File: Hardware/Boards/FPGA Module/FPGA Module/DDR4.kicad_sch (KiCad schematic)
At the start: 36 parts, among them U17 MT40A512M16LY-075:E, U9 TPS74801AWDRC

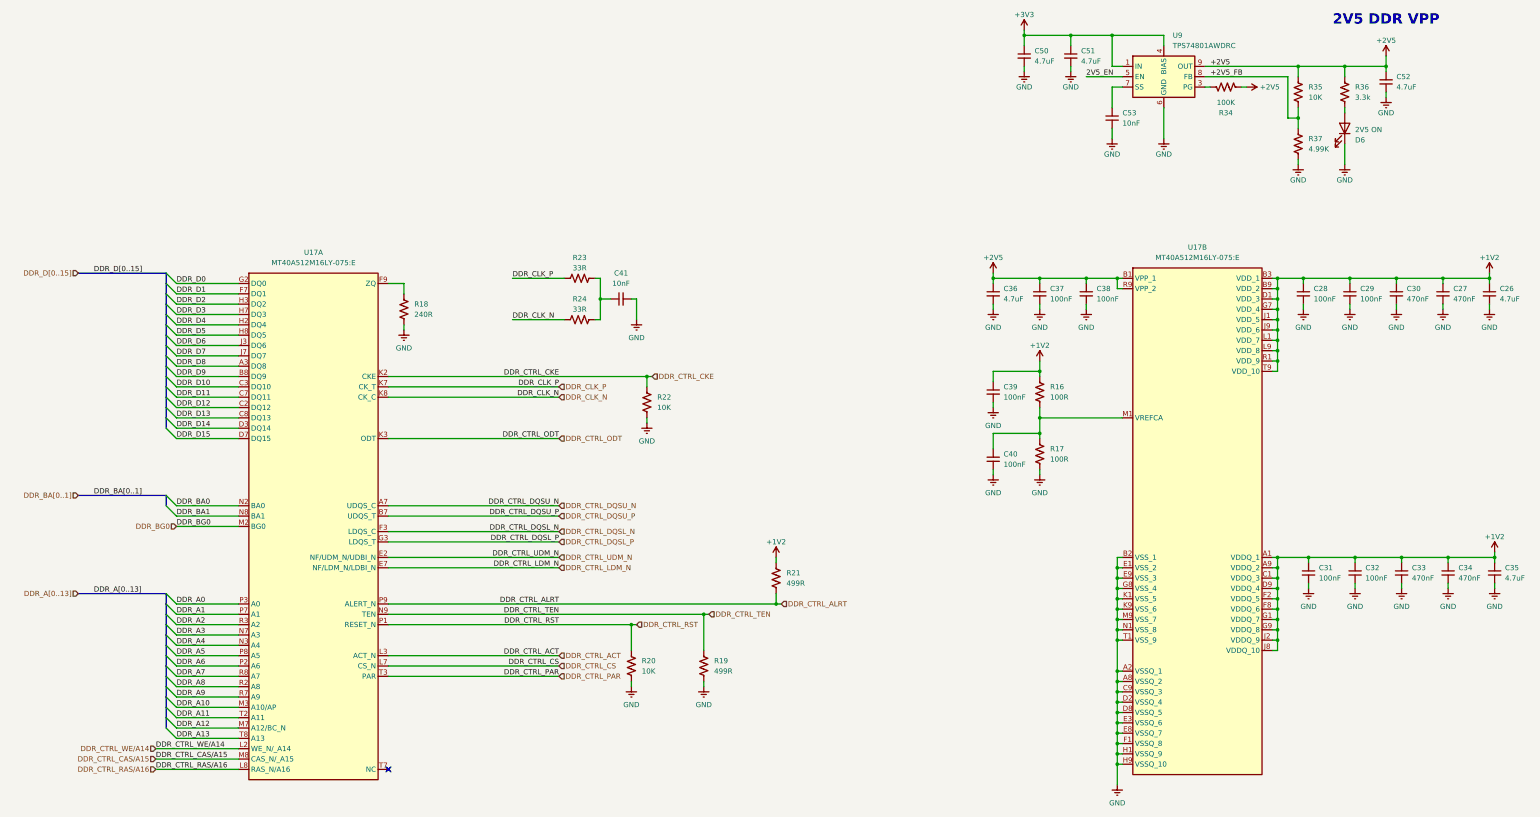
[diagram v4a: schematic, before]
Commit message: Update FPGA Module Netclasses
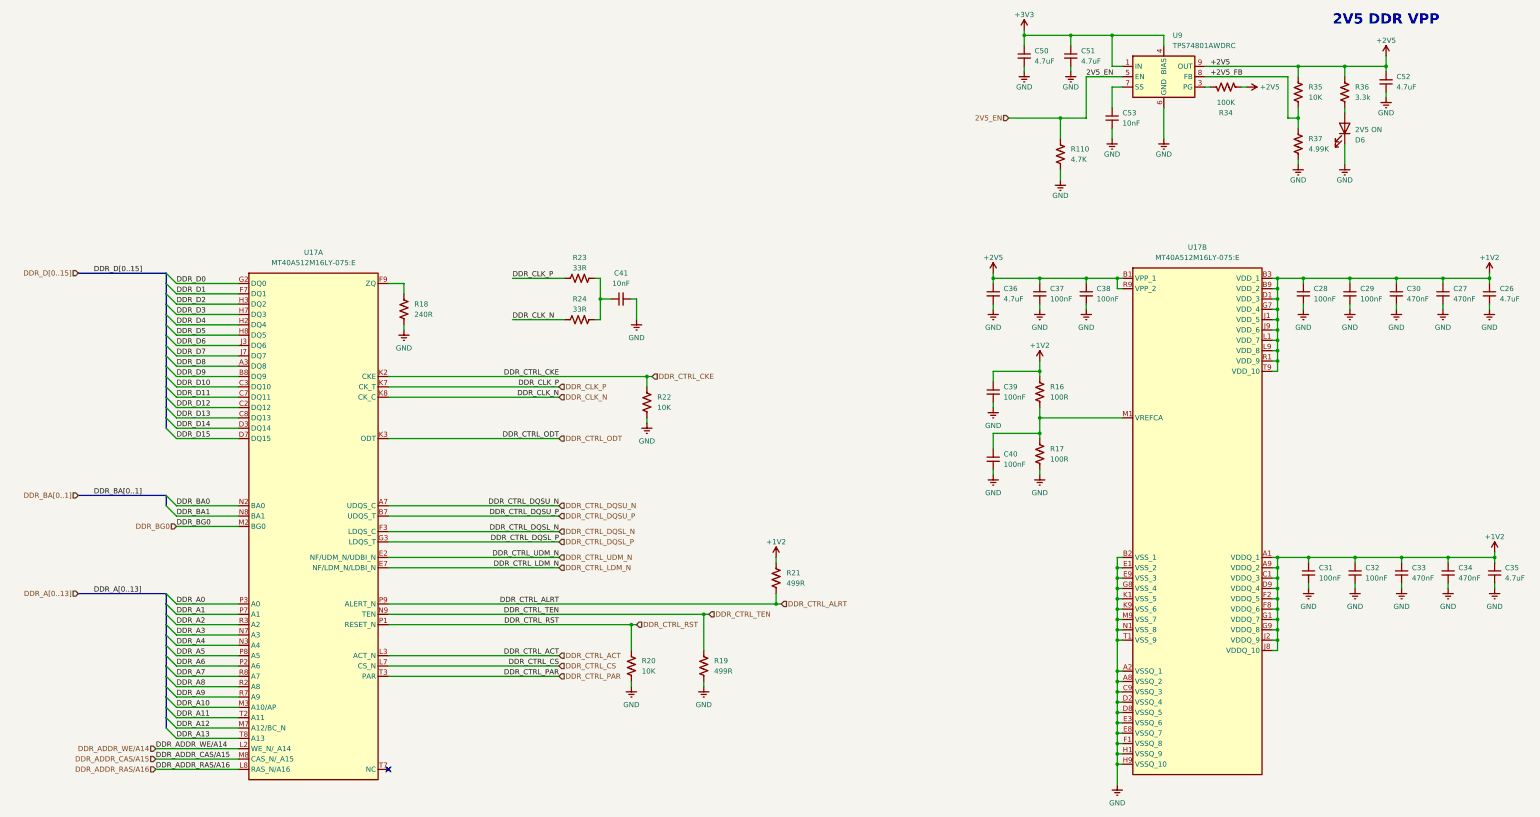
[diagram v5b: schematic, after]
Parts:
- added R110: 4.7K, Resistor_SMD:R_0402_1005Metric, symbol Device:R_US
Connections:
- net 2V5_EN: now also R110.2
- net GND: now also R110.1
- net DDR_CTRL_CAS/A15 renamed DDR_ADDR_CAS/A15
- net DDR_CTRL_RAS/A16 renamed DDR_ADDR_RAS/A16
- net DDR_CTRL_WE/A14 renamed DDR_ADDR_WE/A14
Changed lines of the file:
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@@
 	)
 	(junction
+		(at 279.4 53.34)
+		(diameter 0)
+		(color 0 0 0 0)
+	)
+	(junction
 		(at 293.37 191.77)
 		(diameter 0)
@@
 	(wire
 		(pts
+			(xy 279.4 53.34) (xy 285.75 53.34)
+		)
+		(stroke
+			(width 0)
+			(type default)
+		)
+	)
+	(wire
+		(pts
 			(xy 332.74 166.37) (xy 332.74 168.91)
 		)
@@
 	(wire
 		(pts
+			(xy 266.7 53.34) (xy 279.4 53.34)
+		)
+		(stroke
+			(width 0)
+			(type default)
+		)
+	)
+	(wire
+		(pts
 			(xy 62.23 185.42) (xy 77.47 185.42)
 		)
@@
 	(wire
 		(pts
+			(xy 279.4 66.04) (xy 279.4 68.58)
+		)
+		(stroke
+			(width 0)
+			(type default)
+		)
+	)
+	(wire
+		(pts
 			(xy 337.82 53.34) (xy 337.82 50.8)
 		)
@@
 	(wire
 		(pts
+			(xy 279.4 53.34) (xy 279.4 58.42)
+		)
+		(stroke
+			(width 0)
+			(type default)
+		)
+	)
+	(wire
+		(pts
 			(xy 166.37 102.87) (xy 165.1 102.87)
 		)
@@
 		)
 	)
+	(wire
+		(pts
+			(xy 285.75 53.34) (xy 285.75 43.18)
+		)
+		(stroke
+			(width 0)
+			(type default)
+		)
+	)
 	(bus
 		(pts
@@
 		)
 	)
-	(label "DDR_CTRL_CAS{slash}A15"
+	(label "DDR_ADDR_CAS{slash}A15"
 		(at 57.15 210.82 0)
 		(fields_autoplaced yes)
@@
 		)
 	)
-	(label "DDR_CTRL_RAS{slash}A16"
+	(label "DDR_ADDR_RAS{slash}A16"
 		(at 57.15 213.36 0)
 		(fields_autoplaced yes)
@@
 		)
 	)
-	(label "DDR_CTRL_WE{slash}A14"
+	(label "DDR_ADDR_WE{slash}A14"
 		(at 57.15 208.28 0)
 		(fields_autoplaced yes)
@@
 		)
 	)
-	(hierarchical_label "DDR_CTRL_RAS{slash}A16"
+	(hierarchical_label "DDR_ADDR_RAS{slash}A16"
 		(shape input)
 		(at 57.15 213.36 180)
@@
 		)
 	)
-	(hierarchical_label "DDR_CTRL_CAS{slash}A15"
+	(hierarchical_label "DDR_ADDR_CAS{slash}A15"
 		(shape input)
 		(at 57.15 210.82 180)
@@
 		)
 	)
-	(hierarchical_label "DDR_CTRL_WE{slash}A14"
+	(hierarchical_label "DDR_ADDR_WE{slash}A14"
 		(shape input)
 		(at 57.15 208.28 180)
@@
 		)
 	)
+	(hierarchical_label "2V5_EN"
+		(shape input)
+		(at 266.7 53.34 180)
+		(fields_autoplaced yes)
+		(effects
+			(font
+				(size 1.27 1.27)
+			)
+			(justify right)
+		)
+	)
 	(hierarchical_label "DDR_D[0..15]"
 		(shape input)
@@
 	)
 	(symbol
+		(lib_id "Device:R_US")
+		(at 279.4 62.23 180)
+		(unit 1)
+		(exclude_from_sim no)
+		(in_bom yes)
+		(on_board yes)
+		(dnp no)
+		(fields_autoplaced yes)
+		(property "Reference" "R110"
+			(at 281.94 60.9599 0)
+			(effects
+				(font
+					(size 1.27 1.27)
+				)
+				(justify right)
+			)
+		)
+		(property "Value" "4.7K"
+			(at 281.94 63.4999 0)
+			(effects
+				(font
+					(size 1.27 1.27)
+				)
+				(justify right)
+			)
+		)
+		(property "Footprint" "Resistor_SMD:R_0402_1005Metric"
+			(at 278.384 61.976 90)
+			(effects
+				(font
+					(size 1.27 1.27)
+				)
+				(hide yes)
+			)
+		)
+		(property "Datasheet" "~"
+			(at 279.4 62.23 0)
+			(effects
+				(font
+					(size 1.27 1.27)
+				)
+				(hide yes)
+			)
+		)
+		(property "Description" "Resistor, US symbol"
+			(at 279.4 62.23 0)
+			(effects
+				(font
+					(size 1.27 1.27)
+				)
+				(hide yes)
+			)
+		)
+		(pin "1"
+		)
+		(pin "2"
+		)
+		(instances
+			(project "FPGA Module"
+				(path "/199f10e2-d4b4-4a27-9e84-7b1ce2ae6bf0/0c296310-f788-47f0-8a3f-43c3444563e8/da573161-4ae5-4162-b260-507f695d02e2"
+					(reference "R110")
+					(unit 1)
+				)
+			)
+		)
+	)
+	(symbol
 		(lib_id "power:GND")
 		(at 340.36 168.91 0)
@@
 					(unit 1)
 				)
+			)
+		)
+	)
+	(symbol
+		(lib_id "power:GND")
+		(at 279.4 68.58 0)
+		(mirror y)
+		(unit 1)
+		(exclude_from_sim no)
+		(in_bom yes)
+		(on_board yes)
+		(dnp no)
+		(property "Reference" "#PWR022"
+			(at 279.4 74.93 0)
+			(effects
+				(font
+					(size 1.27 1.27)
+				)
+				(hide yes)
+			)
+		)
+		(property "Value" "GND"
+			(at 279.4 72.39 0)
+			(effects
+				(font
+					(size 1.27 1.27)
+				)
+			)
+		)
+		(property "Footprint" ""
+			(at 279.4 68.58 0)
+			(effects
+				(font
+					(size 1.27 1.27)
+				)
+				(hide yes)
+			)
+		)
+		(property "Datasheet" ""
+			(at 279.4 68.58 0)
+			(effects
+				(font
+					(size 1.27 1.27)
+				)
+				(hide yes)
+			)
+		)
+		(property "Description" "Power symbol creates a global label with name \"GND\" , ground"
+			(at 279.4 68.58 0)
+			(effects
+				(font
+					(size 1.27 1.27)
+				)
+				(hide yes)
+			)
+		)
+		(pin "1"
+		)
+		(instances
+			(project "FPGA Module"
+				(path "/199f10e2-d4b4-4a27-9e84-7b1ce2ae6bf0/0c296310-f788-47f0-8a3f-43c3444563e8/da573161-4ae5-4162-b260-507f695d02e2"
+					(reference "#PWR022")
+					(unit 1)
+				)

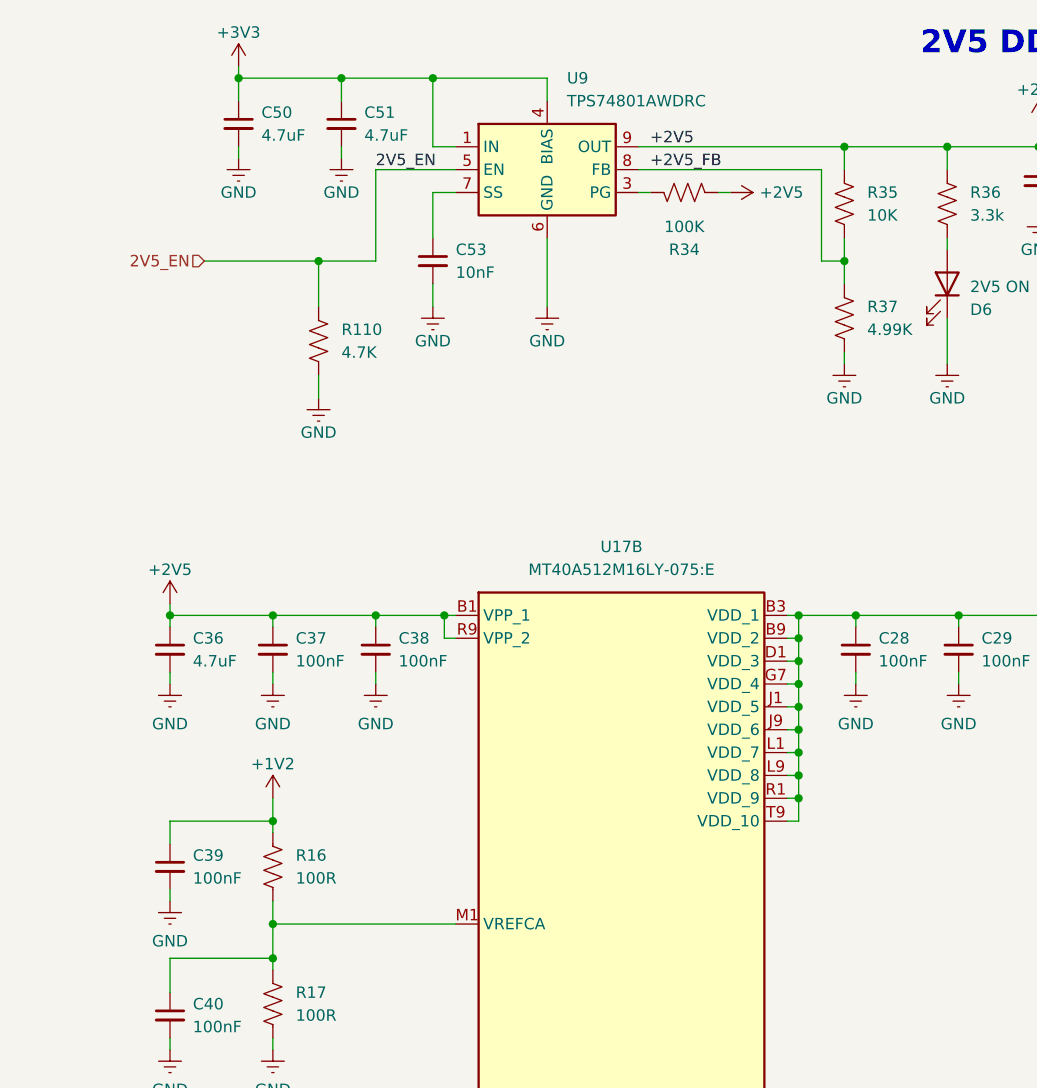
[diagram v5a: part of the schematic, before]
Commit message: FPGA Module sch update
Added 3V3 LDO for MCU and 3V3 EN for DCDC. Also added SPI bus from MCU to FPGA with level shifter
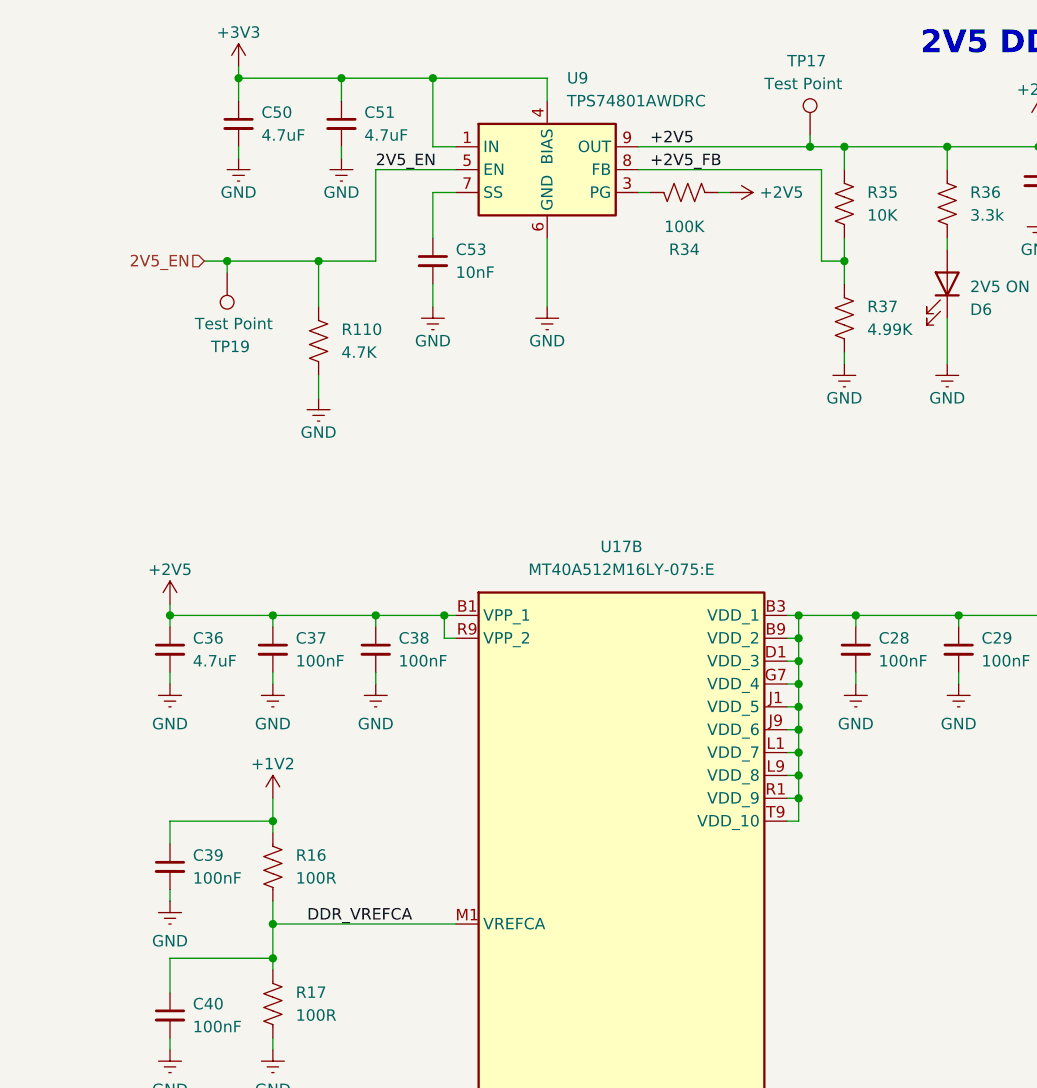
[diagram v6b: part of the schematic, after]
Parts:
- added TP17, TP19: Test Point, FPGA Module:Test Point 0.75mm, symbol Connector:TestPoint
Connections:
- net +2V5: now also TP17.1
- net 2V5_EN: now also TP19.1
- net DDR_VREFCA: now reaches C40.1, R16.1, R17.2, U17.M1 (VREFCA)
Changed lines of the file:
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@@
 	)
 	(junction
+		(at 334.01 40.64)
+		(diameter 0)
+		(color 0 0 0 0)
+	)
+	(junction
 		(at 332.74 176.53)
 		(diameter 0)
@@
 	)
 	(junction
+		(at 269.24 53.34)
+		(diameter 0)
+		(color 0 0 0 0)
+	)
+	(junction
 		(at 293.37 194.31)
 		(diameter 0)
@@
 	(wire
 		(pts
-			(xy 266.7 53.34) (xy 279.4 53.34)
+			(xy 266.7 53.34) (xy 269.24 53.34)
 		)
 		(stroke
@@
 	(wire
 		(pts
+			(xy 269.24 53.34) (xy 269.24 54.61)
+		)
+		(stroke
+			(width 0)
+			(type default)
+		)
+	)
+	(wire
+		(pts
 			(xy 293.37 176.53) (xy 293.37 179.07)
 		)
@@
 	(wire
 		(pts
-			(xy 314.96 40.64) (xy 337.82 40.64)
+			(xy 314.96 40.64) (xy 334.01 40.64)
 		)
 		(stroke
@@
 	(wire
 		(pts
+			(xy 334.01 39.37) (xy 334.01 40.64)
+		)
+		(stroke
+			(width 0)
+			(type default)
+		)
+	)
+	(wire
+		(pts
 			(xy 332.74 173.99) (xy 332.74 176.53)
 		)
@@
 	(wire
 		(pts
+			(xy 334.01 40.64) (xy 337.82 40.64)
+		)
+		(stroke
+			(width 0)
+			(type default)
+		)
+	)
+	(wire
+		(pts
 			(xy 293.37 204.47) (xy 293.37 207.01)
 		)
@@
 	(wire
 		(pts
+			(xy 269.24 53.34) (xy 279.4 53.34)
+		)
+		(stroke
+			(width 0)
+			(type default)
+		)
+	)
+	(wire
+		(pts
 			(xy 114.3 121.92) (xy 156.21 121.92)
 		)
@@
 		)
 	)
+	(label "DDR_VREFCA"
+		(at 278.13 127 0)
+		(fields_autoplaced yes)
+		(effects
+			(font
+				(size 1.27 1.27)
+			)
+			(justify left bottom)
+		)
+	)
 	(label "DDR_D[0..15]"
 		(at 41.91 91.44 0)
@@
 	)
 	(symbol
+		(lib_id "Connector:TestPoint")
+		(at 269.24 54.61 180)
+		(unit 1)
+		(exclude_from_sim no)
+		(in_bom yes)
+		(on_board yes)
+		(dnp no)
+		(property "Reference" "TP19"
+			(at 271.78 62.865 0)
+			(effects
+				(font
+					(size 1.27 1.27)
+				)
+				(justify left)
+			)
+		)
+		(property "Value" "Test Point"
+			(at 274.32 60.325 0)
+			(effects
+				(font
+					(size 1.27 1.27)
+				)
+				(justify left)
+			)
+		)
+		(property "Footprint" "FPGA Module:Test Point 0.75mm"
+			(at 264.16 54.61 0)
+			(effects
+				(font
+					(size 1.27 1.27)
+				)
+				(hide yes)
+			)
+		)
+		(property "Datasheet" "~"
+			(at 264.16 54.61 0)
+			(effects
+				(font
+					(size 1.27 1.27)
+				)
+				(hide yes)
+			)
+		)
+		(property "Description" "test point"
+			(at 269.24 54.61 0)
+			(effects
+				(font
+					(size 1.27 1.27)
+				)
+				(hide yes)
+			)
+		)
+		(pin "1"
+		)
+		(instances
+			(project "FPGA Module"
+				(path "/199f10e2-d4b4-4a27-9e84-7b1ce2ae6bf0/0c296310-f788-47f0-8a3f-43c3444563e8/da573161-4ae5-4162-b260-507f695d02e2"
+					(reference "TP19")
+					(unit 1)
+				)
+			)
+		)
+	)
+	(symbol
 		(lib_id "power:GND")
 		(at 191.77 193.04 0)
@@
 					(unit 1)
 				)
+			)
+		)
+	)
+	(symbol
+		(lib_id "Connector:TestPoint")
+		(at 334.01 39.37 0)
+		(unit 1)
+		(exclude_from_sim no)
+		(in_bom yes)
+		(on_board yes)
+		(dnp no)
+		(property "Reference" "TP17"
+			(at 331.47 31.115 0)
+			(effects
+				(font
+					(size 1.27 1.27)
+				)
+				(justify left)
+			)
+		)
+		(property "Value" "Test Point"
+			(at 328.93 33.655 0)
+			(effects
+				(font
+					(size 1.27 1.27)
+				)
+				(justify left)
+			)
+		)
+		(property "Footprint" "FPGA Module:Test Point 0.75mm"
+			(at 339.09 39.37 0)
+			(effects
+				(font
+					(size 1.27 1.27)
+				)
+				(hide yes)
+			)
+		)
+		(property "Datasheet" "~"
+			(at 339.09 39.37 0)
+			(effects
+				(font
+					(size 1.27 1.27)
+				)
+				(hide yes)
+			)
+		)
+		(property "Description" "test point"
+			(at 334.01 39.37 0)
+			(effects
+				(font
+					(size 1.27 1.27)
+				)
+				(hide yes)
+			)
+		)
+		(pin "1"
+		)
+		(instances
+			(project "FPGA Module"
+				(path "/199f10e2-d4b4-4a27-9e84-7b1ce2ae6bf0/0c296310-f788-47f0-8a3f-43c3444563e8/da573161-4ae5-4162-b260-507f695d02e2"
+					(reference "TP17")
+					(unit 1)
+				)
